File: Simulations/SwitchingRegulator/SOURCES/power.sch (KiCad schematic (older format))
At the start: 8 parts

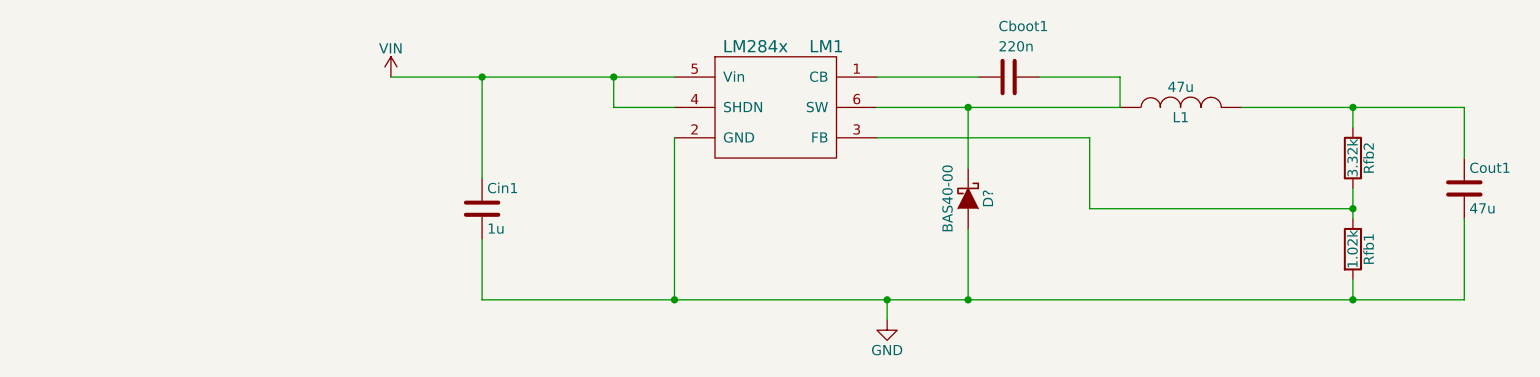
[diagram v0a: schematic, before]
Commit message: Added connector to power supply
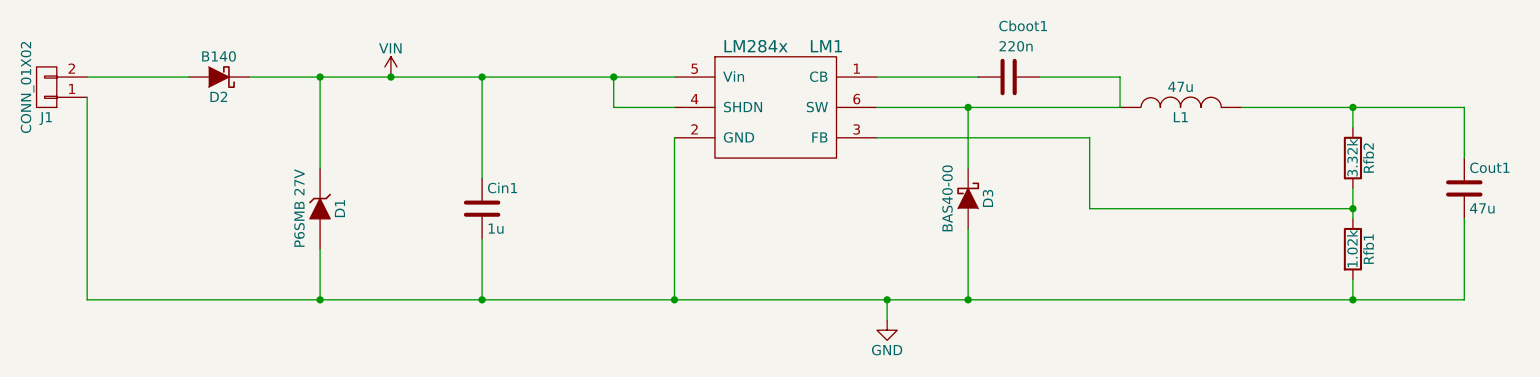
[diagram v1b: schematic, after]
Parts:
- added D1: P6SMB 27V, fdsp_diode:SMB, symbol ZENER
- added D2: B140, fdsp_diode:SMA, symbol D_Schottky
- added J1: CONN_01X02, fdsp_connector:RIACON101-2, symbol CONN_01X02
- gave numbers to parts that had none: 1
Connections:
- net GND: now also D1.2 (A), J1.1 (P1)
- net VIN: now also D1.1 (K), D2.1 (K)
- new net: D2.2 (A), J1.2 (P2)
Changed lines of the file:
@@
 	5900 5450 5900 5350
 Wire Wire Line
-	3900 5350 8750 5350
+	1950 5350 8750 5350
 Wire Wire Line
 	8200 5350 8200 5250
@@
 Connection ~ 3900 4250
 Wire Wire Line
-	3450 4250 4850 4250
+	2750 4250 4850 4250
 $Comp
-L BAS40-00 D?
+L BAS40-00 D3
 U 1 1 592B508F
 P 6300 4850
-F 0 "D?" H 6300 4950 50  0000 C CNN
+F 0 "D3" H 6300 4950 50  0000 C CNN
 F 1 "BAS40-00" H 6300 4750 50  0000 C CNN
 F 2 "TO_SOT_Packages_SMD:SOT-23" H 6300 4650 20  0001 C CNN
@@
 	0    1    1    0
 $EndComp
+$Comp
+L ZENER D1
+U 1 1 592B0AB6
+P 3100 4900
+F 0 "D1" H 3100 5000 50  0000 C CNN
+F 1 "P6SMB 27V" H 3100 4800 50  0000 C CNN
+F 2 "fdsp_diode:SMB" H 3100 4900 60  0001 C CNN
+F 3 "http://www.mouser.com/ds/2/54/6smb-778327.pdf" H 3100 4900 60  0001 C CNN
+	1    3100 4900
+	0    1    1    0
+$EndComp
+$Comp
+L D_Schottky D2
+U 1 1 592B0C13
+P 2600 4250
+F 0 "D2" H 2600 4350 50  0000 C CNN
+F 1 "B140" H 2600 4150 50  0000 C CNN
+F 2 "fdsp_diode:SMA" H 2600 4250 60  0001 C CNN
+F 3 "http://www.mouser.com/ds/2/115/ds13002-60388.pdf" H 2600 4250 60  0001 C CNN
+	1    2600 4250
+	-1   0    0    1
+$EndComp
+$Comp
+L CONN_01X02 J1
+U 1 1 592B0D49
+P 1750 4300
+F 0 "J1" H 1750 4450 50  0000 C CNN
+F 1 "CONN_01X02" V 1850 4300 50  0000 C CNN
+F 2 "fdsp_connector:RIACON101-2" H 1750 4300 50  0001 C CNN
+F 3 "" H 1750 4300 50  0001 C CNN
+	1    1750 4300
+	-1   0    0    1
+$EndComp
+Wire Wire Line
+	1950 5350 1950 4350
+Connection ~ 3900 5350
+Wire Wire Line
+	3100 5100 3100 5350
+Connection ~ 3100 5350
+Wire Wire Line
+	2450 4250 1950 4250
+Connection ~ 3450 4250
+Wire Wire Line
+	3100 4700 3100 4250
+Connection ~ 3100 4250
 $EndSCHEMATC
